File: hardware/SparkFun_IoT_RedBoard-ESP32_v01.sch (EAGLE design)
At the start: 113 parts, among them J1 5.5x2.1mm Barrel, J13 QWIIC_RIGHT_ANGLE, J15 MICRO-SD-PUSH-PUSH-EXT-PIN, J2 USB C, J3 USB_SOLDER_PADS, J5 M10NO_SILK, Q1 MBT3904DW1T1, Q11 20V/4.2A/52mΩ/1.4W, Q13 20V/4.2A/52mΩ/1.4W, Q3 20V/4.2A/52mΩ/1.4W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

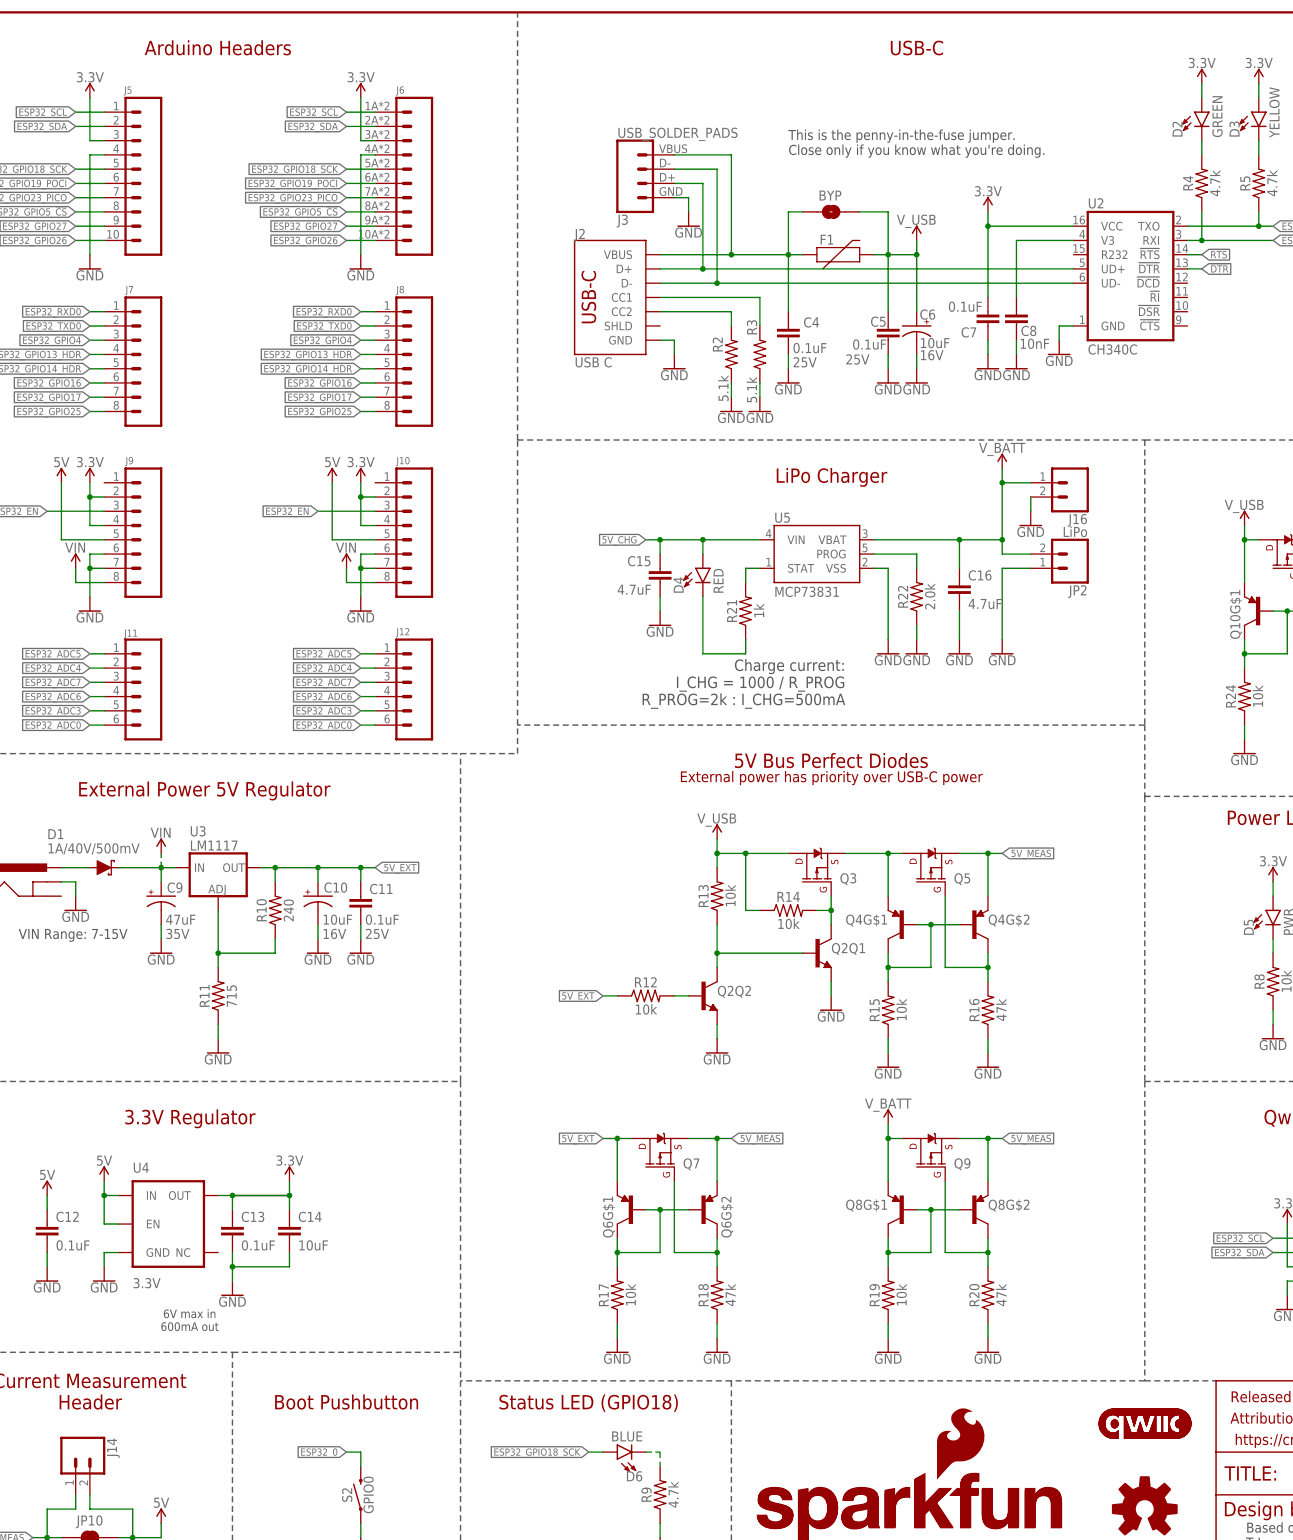
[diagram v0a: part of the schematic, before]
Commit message: Implemented changes suggested by Pete Lewis.
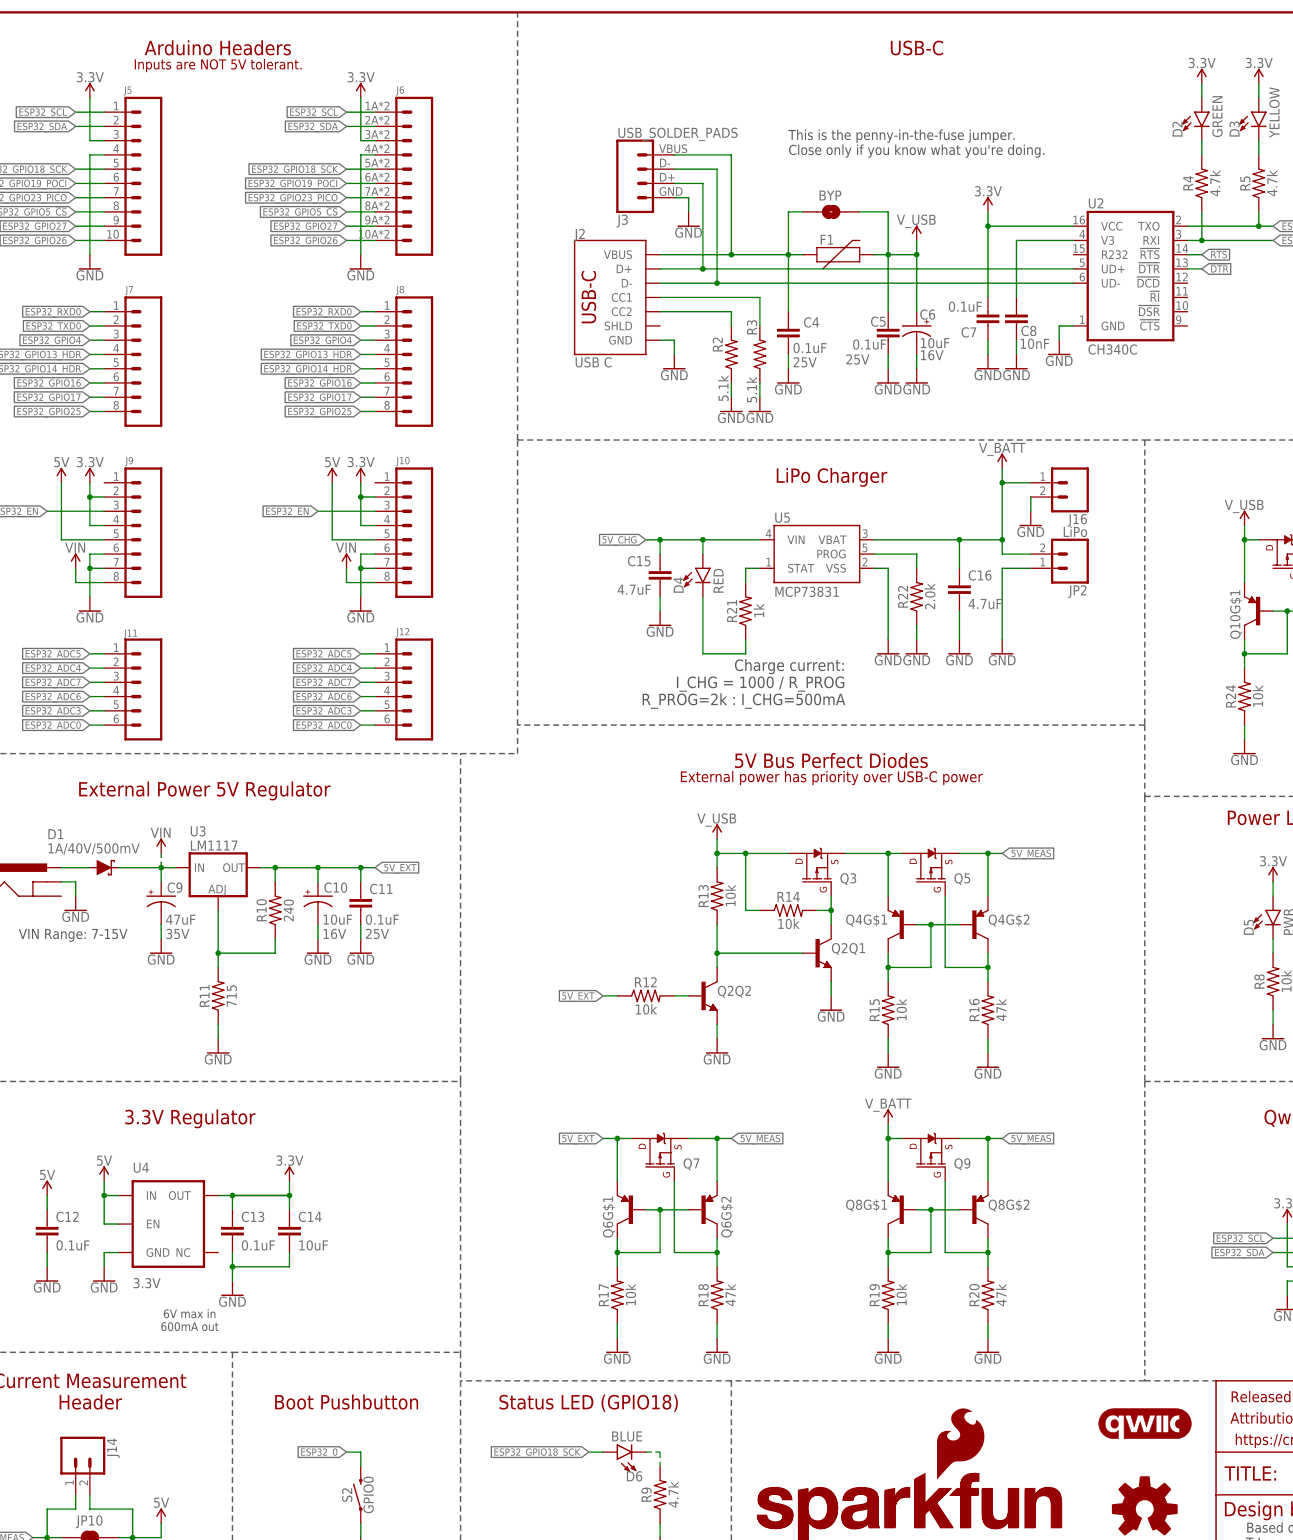
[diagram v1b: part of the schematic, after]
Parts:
- removed LOGO4: QWIIC_LOGO_5MM, SparkFun-Aesthetics:QWIIC_LOGO_5MM
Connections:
- net VUSB renamed VBUS
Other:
- note added: "Inputs are NOT 5V tolerant."
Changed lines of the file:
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@@
 <part name="LOGO2" library="SparkFun-Aesthetics" deviceset="QWIIC_LOGO" device="_5MM"/>
 <part name="LOGO3" library="SparkFun-Aesthetics" deviceset="OSHW-LOGO" device="MINI"/>
-<part name="LOGO4" library="SparkFun-Aesthetics" deviceset="QWIIC_LOGO" device="_5MM"/>
 <part name="SUPPLY28" library="SparkFun-PowerSymbols" deviceset="VIN" device=""/>
 <part name="LOGO5" library="SparkFun-Aesthetics" deviceset="SPECIAL_INSTRUCTIONS" device="-ORDERING"/>
@@
 <wire x1="154.94" y1="40.64" x2="154.94" y2="0" width="0.254" layer="97" style="longdash"/>
 <wire x1="243.84" y1="35.56" x2="243.84" y2="0" width="0.254" layer="97" style="longdash"/>
+<text x="152.4" y="269.24" size="1.778" layer="94" font="vector" ratio="11" align="bottom-center">Inputs are NOT 5V tolerant.</text>
 </plain>
 <instances>
@@
 <instance part="LOGO2" gate="G$1" x="317.5" y="27.94" smashed="yes"/>
 <instance part="LOGO3" gate="G$1" x="317.5" y="12.7" smashed="yes"/>
-<instance part="LOGO4" gate="G$1" x="317.5" y="27.94" smashed="yes"/>
 <instance part="SUPPLY28" gate="G$1" x="142.24" y="129.54" smashed="yes">
 <attribute name="VALUE" x="142.24" y="132.334" size="1.778" layer="96" align="bottom-center"/>
@@
 </segment>
 </net>
-<net name="VUSB" class="1">
+<net name="VBUS" class="1">
 <segment>
 <pinref part="C4" gate="G$1" pin="1"/>

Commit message: Updated design per Engineering checklist.
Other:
- note added: "Close jumper to enable !GAUGE_ALERT! to be connected to ESP32 GPIO pin 4"
- note added: "I2C Address: 0x36"
- note added: "Open jumper to measure board current on J14"
- note added: "Open jumper to remove I2C pullups."
- note added: "Open jumpers to isolate GPIO13 and GPIO14 from the JTAG header"
- moved on the sheet: J4, JP13, JP14, TP1

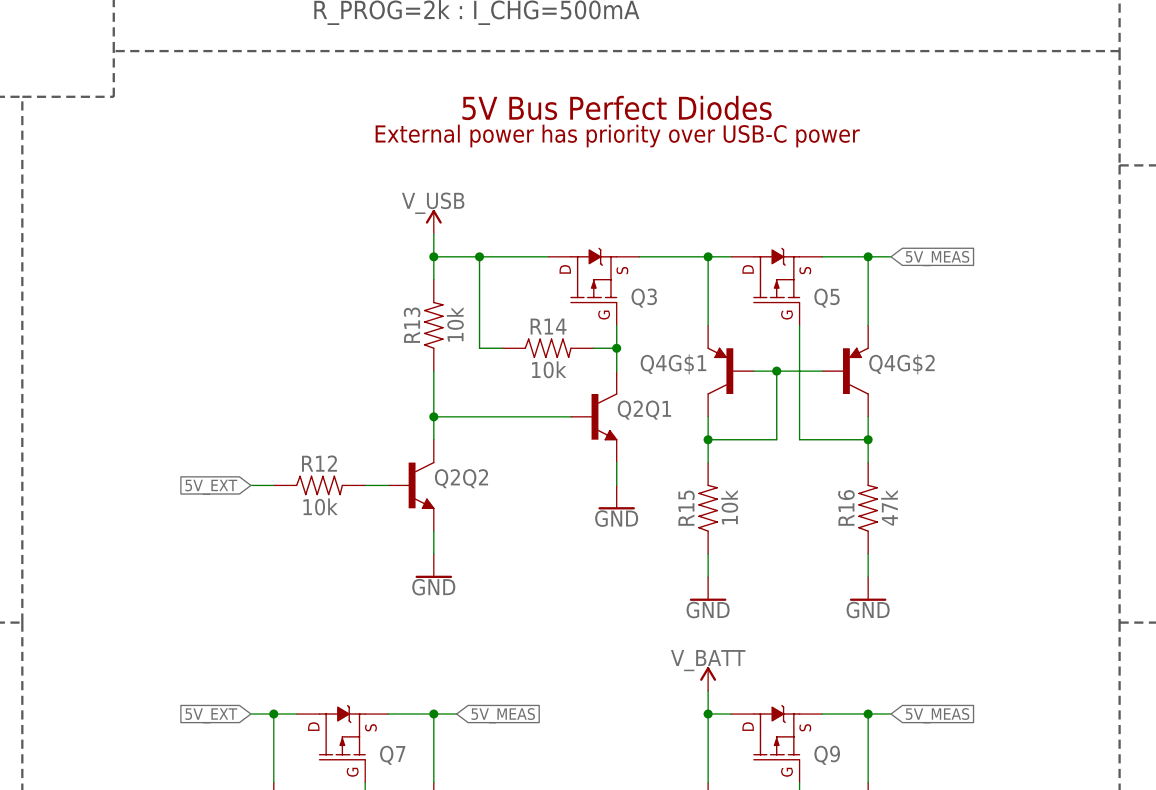
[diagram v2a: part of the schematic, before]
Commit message: Flipped Q3, added 100R resistor to Q3's gate and changed panel to 2x2 boards
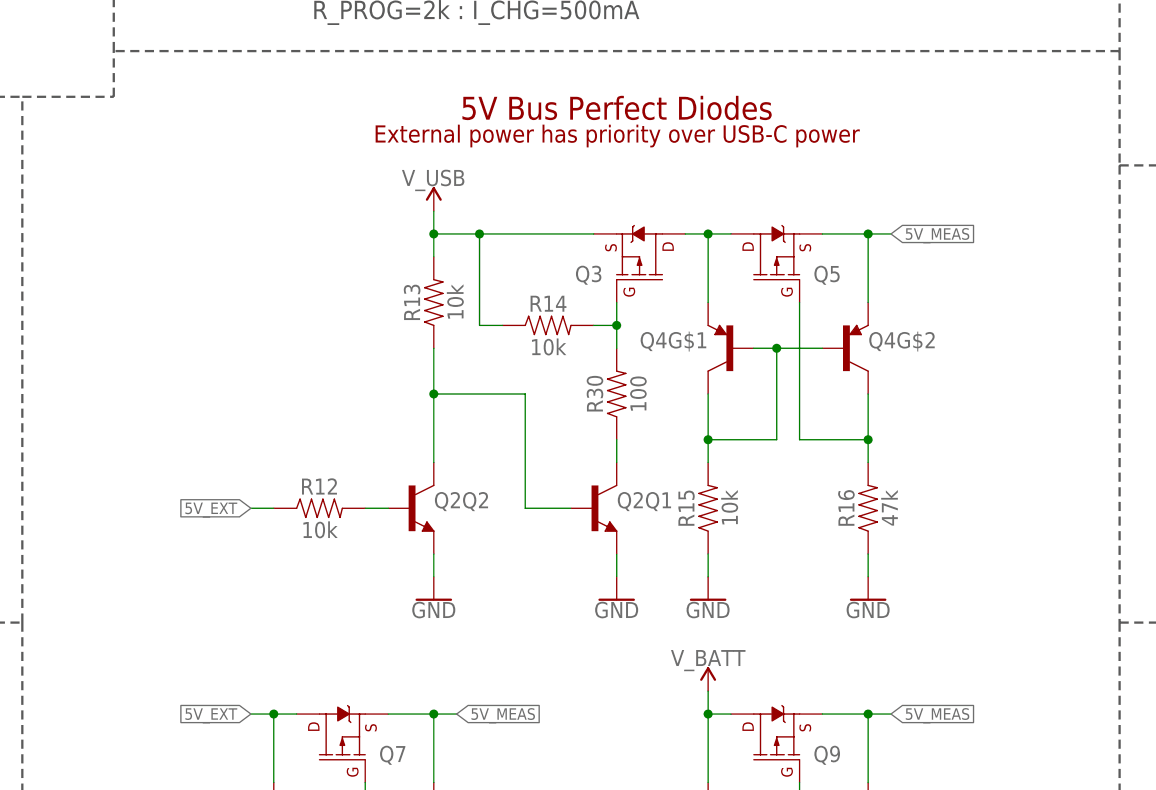
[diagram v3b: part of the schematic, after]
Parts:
- added R30: 100, SparkFun-Resistors:100OHM-0603-1/10W-1%
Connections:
- removed net N$19: Q2Q1.C, Q3.G, R14.2
- new net N$11: Q2Q1.C, R30.1
- new net N$9: Q3.G, R14.2, R30.2
- net VUSB_PROT: now also Q3.D; no longer Q3.S
- net V_USB: now also Q3.S; no longer Q3.D
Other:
- moved on the sheet: Q2Q1, Q2Q2, Q3, Q4G$1, Q4G$2, Q5, R12, R13, R14
